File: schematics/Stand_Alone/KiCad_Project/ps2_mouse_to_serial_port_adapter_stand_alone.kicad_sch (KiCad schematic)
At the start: 24 parts, among them J1 Barrel Jack 2.1 mm, J2 DB9 Female, J3 Mini-DIN-6, Q1 BC547, SW1 1C2P, U1 74LS00, U2 L78L05, U3 L7805

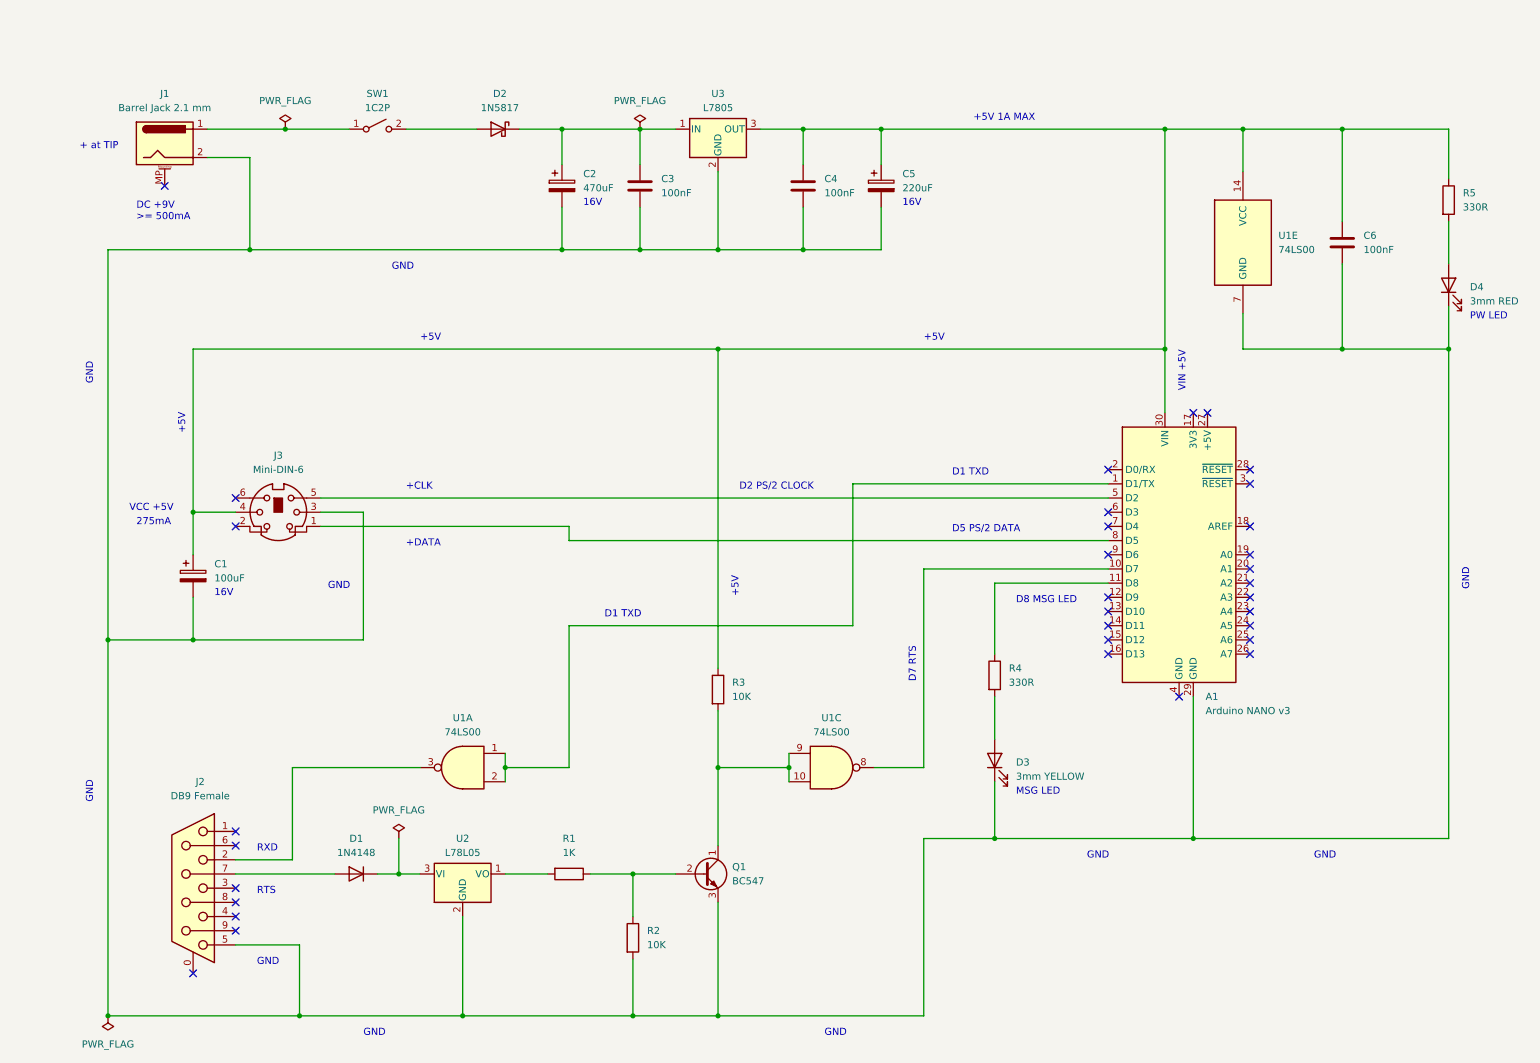
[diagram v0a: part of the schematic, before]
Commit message: v1.5.0
- Ajustadas las placas "Stand alone" y "In-a-box" al tamaño standard de
  90x70 mm.
- Añadidas a estas placas las zonas de relleno a masa (GND).
- Añadidas las serigrafias con los valores de todos los componentes en todas
  las versiones de las placas.
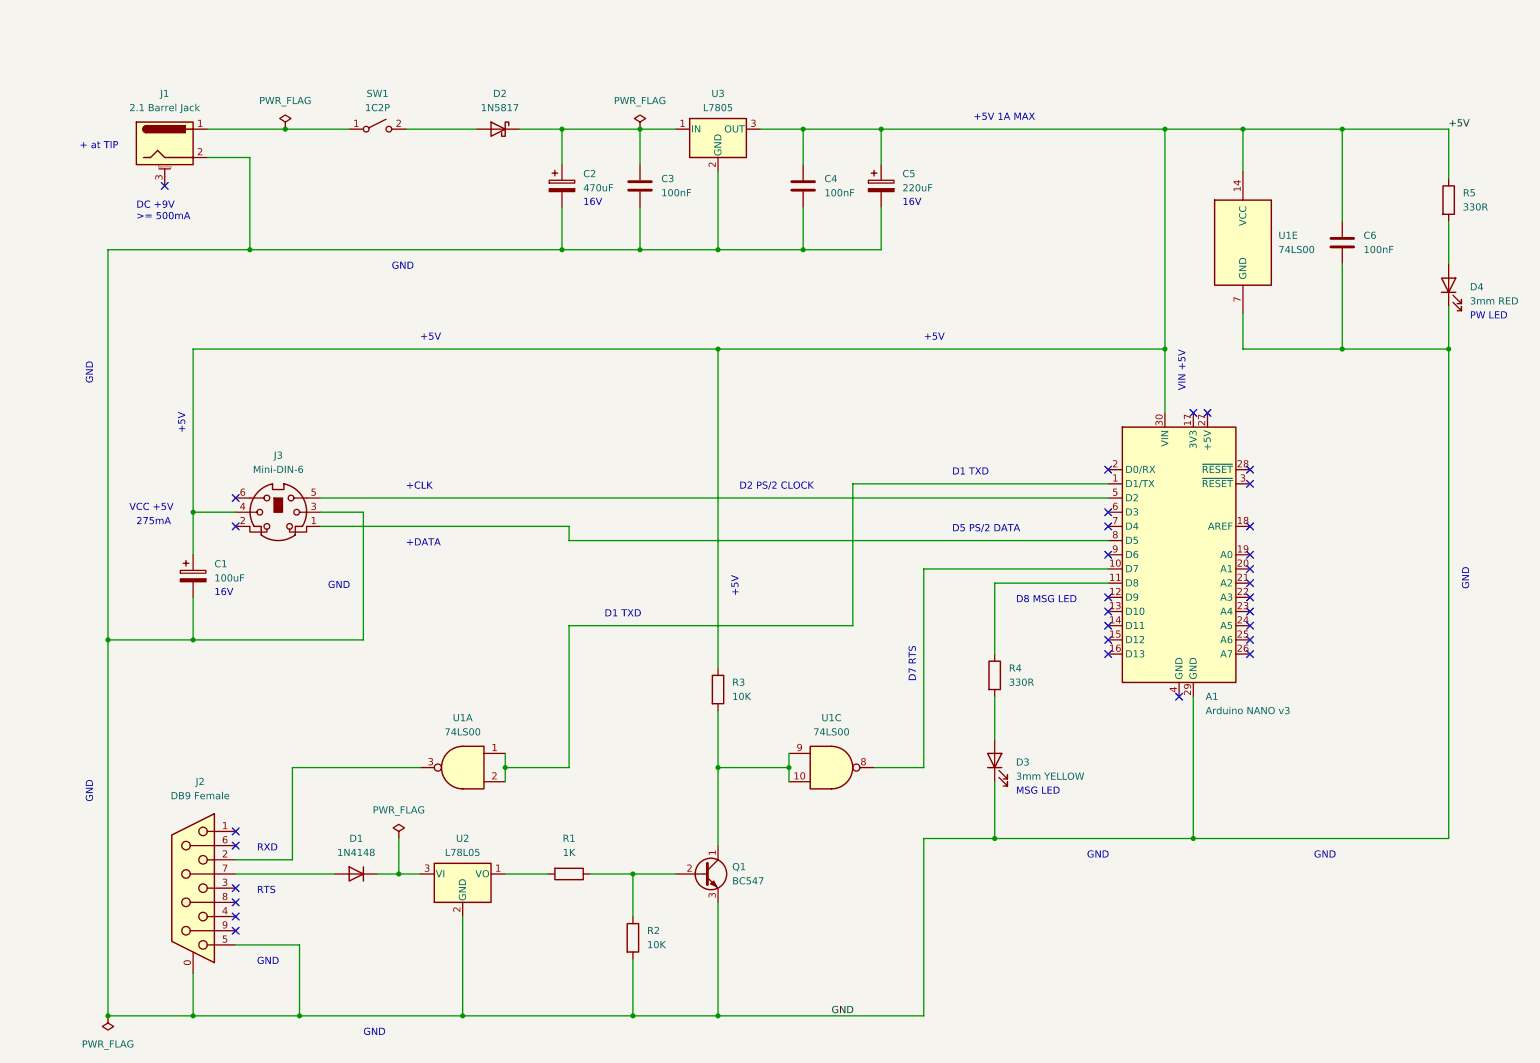
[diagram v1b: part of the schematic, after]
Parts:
- removed J1: Barrel Jack 2.1 mm, Connector_BarrelJack:BarrelJack_Horizontal, symbol Connector:Barrel_Jack_MountingPin
- added J1: 2.1 Barrel Jack, Connector_BarrelJack:BarrelJack_Kycon_KLDX-0202-xC_Horizontal, symbol CustomSymbols:Barrel_Jack_MountingPin
- U1: footprint (none) -> Package_DIP:DIP-14_W7.62mm_Socket
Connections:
- net +5V: now reaches A1.30 (VIN), C1.1, C4.1, C5.1, C6.1, J3.4, R3.1, R5.1, U1.14 (VCC), U3.3 (OUT)
- net GND: now reaches A1.29 (GND), C1.2, C2.2, C3.2, C4.2, C5.2, C6.2, D3.1 (K), D4.1 (K), J2.5, J3.3, Q1.3 (E), R2.2, U1.7 (GND), U2.2 (GND), U3.2 (GND)
- net GND: now also J2.0 (PAD), J1.2
- net at SW1.1 (A): now also J1.1
- no-connect marks 39 -> 38
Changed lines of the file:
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@@
   (title_block
     (title "PS/2 Mouse  to Serial Port Adapter")
-    (date "2023-08-12")
-    (rev "3")
+    (date "2023-08-13")
+    (rev "4")
     (company "Cesar Rincon")
     (comment 1 "NightFox & Co.")
@@
   (junction (at 212.09 64.77) (diameter 0) (color 0 0 0 0)
   )
+  (junction (at 38.1 184.15) (diameter 0) (color 0 0 0 0)
+  )
   (junction (at 181.61 152.4) (diameter 0) (color 0 0 0 0)
   )
@@
   (no_connect (at 219.71 76.2))
   (no_connect (at 227.33 114.3))
-  (no_connect (at 33.02 35.56))
   (no_connect (at 227.33 104.14))
   (no_connect (at -111.76 2.54))
@@
   (no_connect (at 201.93 111.76))
   (no_connect (at 214.63 127))
+  (no_connect (at 33.02 35.56))
   (no_connect (at -127 25.4))
   (no_connect (at 227.33 101.6))
@@
   (no_connect (at 201.93 101.6))
   (no_connect (at -111.76 27.94))
-  (no_connect (at 38.1 176.53))
   (no_connect (at 201.93 116.84))
   (no_connect (at 45.72 96.52))
@@
     (stroke (width 0) (type default))
   )
+  (wire (pts (xy 38.1 176.53) (xy 38.1 184.15))
+    (stroke (width 0) (type default))
+  )
   (wire (pts (xy 55.88 139.7) (xy 78.74 139.7))
     (stroke (width 0) (type default))
@@
     (stroke (width 0) (type default))
   )
+  (wire (pts (xy 48.26 30.48) (xy 48.26 46.99))
+    (stroke (width 0) (type default))
+  )
   (wire (pts (xy 104.14 46.99) (xy 118.11 46.99))
     (stroke (width 0) (type default))
@@
     (stroke (width 0) (type default))
   )
+  (wire (pts (xy 38.1 184.15) (xy 57.15 184.15))
+    (stroke (width 0) (type default))
+  )
   (wire (pts (xy 201.93 106.68) (xy 181.61 106.68))
     (stroke (width 0) (type default))
@@
     (stroke (width 0) (type default))
   )
-  (wire (pts (xy 22.86 184.15) (xy 57.15 184.15))
+  (wire (pts (xy 22.86 184.15) (xy 38.1 184.15))
     (stroke (width 0) (type default))
   )
@@
     (stroke (width 0) (type default))
   )
-  (wire (pts (xy 48.26 30.48) (xy 48.26 46.99))
-    (stroke (width 0) (type default))
-  )
   (wire (pts (xy 212.09 25.4) (xy 212.09 64.77))
     (stroke (width 0) (type default))
@@
     (effects (font (size 1.27 1.27)) (justify left bottom))
   )
-  (text "GND" (at 151.13 187.96 0)
-    (effects (font (size 1.27 1.27)) (justify left bottom))
-  )
   (text "GND" (at 49.53 175.26 0)
     (effects (font (size 1.27 1.27)) (justify left bottom))
@@
     (effects (font (size 1.27 1.27)) (justify left bottom))
   )
+  (label "+5V" (at 262.89 25.4 0) (fields_autoplaced)
+    (effects (font (size 1.27 1.27)) (justify left bottom))
+  )
+  (label "GND" (at 152.4 184.15 0) (fields_autoplaced)
+    (effects (font (size 1.27 1.27)) (justify left bottom))
+  )
   (symbol (lib_id "74xx:74LS00") (at -119.38 2.54 0) (unit 2)
     (in_bom yes) (on_board yes) (dnp no) (fields_autoplaced)
@@
       (effects (font (size 1.27 1.27)))
     )
-    (property "Footprint" "" (at -119.38 2.54 0)
+    (property "Footprint" "Package_DIP:DIP-14_W7.62mm_Socket" (at -119.38 2.54 0)
       (effects (font (size 1.27 1.27)) hide)
     )
@@
     )
   )
-  (symbol (lib_id "Connector:Barrel_Jack_MountingPin") (at 33.02 27.94 0) (unit 1)
-    (in_bom yes) (on_board yes) (dnp no) (fields_autoplaced)
-    (property "Reference" "J1" (at 33.02 19.05 0)
-      (effects (font (size 1.27 1.27)))
-    )
-    (property "Value" "Barrel Jack 2.1 mm" (at 33.02 21.59 0)
-      (effects (font (size 1.27 1.27)))
-    )
-    (property "Footprint" "Connector_BarrelJack:BarrelJack_Horizontal" (at 34.29 28.956 0)
-      (effects (font (size 1.27 1.27)) hide)
-    )
-    (property "Datasheet" "~" (at 34.29 28.956 0)
-      (effects (font (size 1.27 1.27)) hide)
-    )
-    (pin "1")
-    (pin "2")
-    (pin "MP")
-    (instances
-      (project "ps2_mouse_to_serial_port_adapter_stand_alone"
-        (path "/a7ffaf24-5f7f-4c3c-9493-bf517f6435f3"
-          (reference "J1") (unit 1)
-        )
-      )
-    )
-  )
   (symbol (lib_id "Connector:Mini-DIN-6") (at 53.34 93.98 0) (unit 1)
     (in_bom yes) (on_board yes) (dnp no) (fields_autoplaced)
@@
       (effects (font (size 1.27 1.27)))
     )
-    (property "Footprint" "" (at -119.38 27.94 0)
+    (property "Footprint" "Package_DIP:DIP-14_W7.62mm_Socket" (at -119.38 27.94 0)
       (effects (font (size 1.27 1.27)) hide)
     )
@@
         )
       )
+    )
+  )
+  (symbol (lib_id "CustomSymbols:Barrel_Jack_MountingPin") (at 33.02 27.94 0) (unit 1)
+    (in_bom yes) (on_board yes) (dnp no) (fields_autoplaced)
+    (property "Reference" "J1" (at 33.02 19.05 0)
+      (effects (font (size 1.27 1.27)))
+    )
+    (property "Value" "2.1 Barrel Jack" (at 33.02 21.59 0)
+      (effects (font (size 1.27 1.27)))
+    )
+    (property "Footprint" "Connector_BarrelJack:BarrelJack_Kycon_KLDX-0202-xC_Horizontal" (at 34.29 28.956 0)
+      (effects (font (size 1.27 1.27)) hide)
+    )
+    (property "Datasheet" "~" (at 34.29 28.956 0)
+      (effects (font (size 1.27 1.27)) hide)
+    )
+    (pin "1")
+    (pin "2")
+    (pin "3")
+    (instances
+      (project "ps2_mouse_to_serial_port_adapter_stand_alone"
+        (path "/a7ffaf24-5f7f-4c3c-9493-bf517f6435f3"
+          (reference "J1") (unit 1)
+        )
+      )

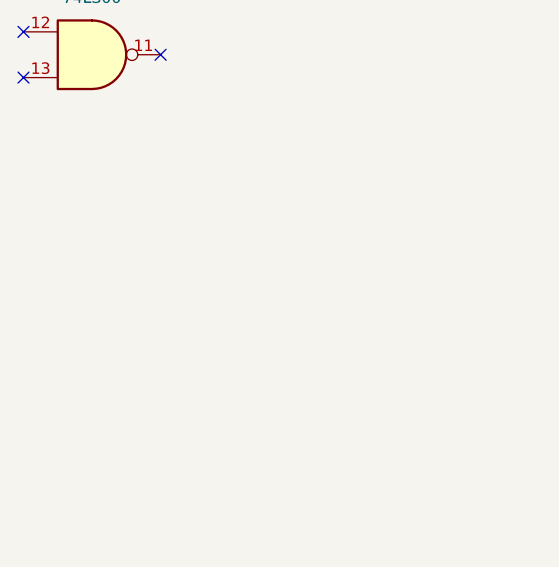
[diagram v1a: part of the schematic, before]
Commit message: v1.5.1
- Arreglada la serigrafía del conector MINI-DIN-6 (PS/2), la cual se superponía en algunas zonas de soldado.
- En todas las placas se añade el símbolo de los agujeros de montaje con el tamaño estándar M3.
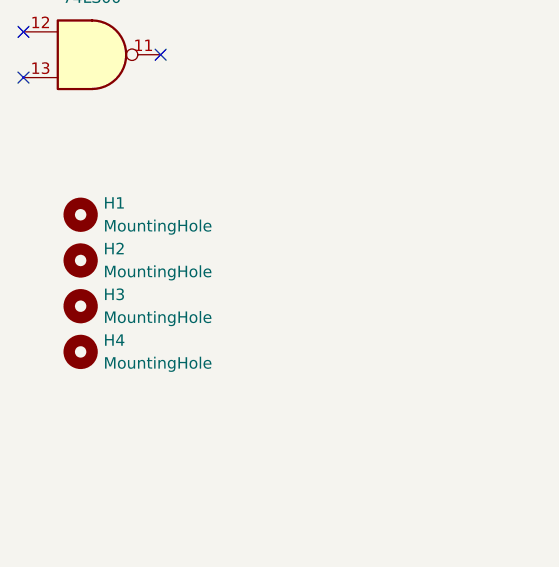
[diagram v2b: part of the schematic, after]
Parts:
- added H1, H2, H3, H4: MountingHole, MountingHole:MountingHole_3.2mm_M3, symbol Mechanical:MountingHole
- J3: footprint CustomFootPrints:Conn_Mini_DIN_6pin -> ProjectLibrary:Connector_Mini_DIN_6pin
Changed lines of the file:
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@@
   (title_block
     (title "PS/2 Mouse  to Serial Port Adapter")
-    (date "2023-08-13")
-    (rev "4")
+    (date "2023-08-14")
+    (rev "5")
     (company "Cesar Rincon")
     (comment 1 "NightFox & Co.")
@@
     )
   )
+  (symbol (lib_id "Mechanical:MountingHole") (at -120.65 50.8 0) (unit 1)
+    (in_bom yes) (on_board yes) (dnp no) (fields_autoplaced)
+    (property "Reference" "H2" (at -118.11 49.53 0)
+      (effects (font (size 1.27 1.27)) (justify left))
+    )
+    (property "Value" "MountingHole" (at -118.11 52.07 0)
+      (effects (font (size 1.27 1.27)) (justify left))
+    )
+    (property "Footprint" "MountingHole:MountingHole_3.2mm_M3" (at -120.65 50.8 0)
+      (effects (font (size 1.27 1.27)) hide)
+    )
+    (property "Datasheet" "~" (at -120.65 50.8 0)
+      (effects (font (size 1.27 1.27)) hide)
+    )
+    (instances
+      (project "ps2_mouse_to_serial_port_adapter_stand_alone"
+        (path "/a7ffaf24-5f7f-4c3c-9493-bf517f6435f3"
+          (reference "H2") (unit 1)
+        )
+      )
+    )
+  )
   (symbol (lib_id "Diode:1N5817") (at 92.71 25.4 0) (mirror y) (unit 1)
     (in_bom yes) (on_board yes) (dnp no) (fields_autoplaced)
@@
       (effects (font (size 1.27 1.27)))
     )
-    (property "Footprint" "CustomFootPrints:Conn_Mini_DIN_6pin" (at 53.34 93.98 0)
+    (property "Footprint" "ProjectLibrary:Connector_Mini_DIN_6pin" (at 53.34 93.98 0)
       (effects (font (size 1.27 1.27)) hide)
     )
@@
     )
   )
+  (symbol (lib_id "Mechanical:MountingHole") (at -120.65 45.72 0) (unit 1)
+    (in_bom yes) (on_board yes) (dnp no) (fields_autoplaced)
+    (property "Reference" "H1" (at -118.11 44.45 0)
+      (effects (font (size 1.27 1.27)) (justify left))
+    )
+    (property "Value" "MountingHole" (at -118.11 46.99 0)
+      (effects (font (size 1.27 1.27)) (justify left))
+    )
+    (property "Footprint" "MountingHole:MountingHole_3.2mm_M3" (at -120.65 45.72 0)
+      (effects (font (size 1.27 1.27)) hide)
+    )
+    (property "Datasheet" "~" (at -120.65 45.72 0)
+      (effects (font (size 1.27 1.27)) hide)
+    )
+    (instances
+      (project "ps2_mouse_to_serial_port_adapter_stand_alone"
+        (path "/a7ffaf24-5f7f-4c3c-9493-bf517f6435f3"
+          (reference "H1") (unit 1)
+        )
+      )
+    )
+  )
   (symbol (lib_id "Device:LED") (at 181.61 138.43 90) (unit 1)
     (in_bom yes) (on_board yes) (dnp no) (fields_autoplaced)
@@
         (path "/a7ffaf24-5f7f-4c3c-9493-bf517f6435f3"
           (reference "D3") (unit 1)
+        )
+      )
+    )
+  )
+  (symbol (lib_id "Mechanical:MountingHole") (at -120.65 55.88 0) (unit 1)
+    (in_bom yes) (on_board yes) (dnp no) (fields_autoplaced)
+    (property "Reference" "H3" (at -118.11 54.61 0)
+      (effects (font (size 1.27 1.27)) (justify left))
+    )
+    (property "Value" "MountingHole" (at -118.11 57.15 0)
+      (effects (font (size 1.27 1.27)) (justify left))
+    )
+    (property "Footprint" "MountingHole:MountingHole_3.2mm_M3" (at -120.65 55.88 0)
+      (effects (font (size 1.27 1.27)) hide)
+    )
+    (property "Datasheet" "~" (at -120.65 55.88 0)
+      (effects (font (size 1.27 1.27)) hide)
+    )
+    (instances
+      (project "ps2_mouse_to_serial_port_adapter_stand_alone"
+        (path "/a7ffaf24-5f7f-4c3c-9493-bf517f6435f3"
+          (reference "H3") (unit 1)
         )
       )
@@
         )
       )
+    )
+  )
+  (symbol (lib_id "Mechanical:MountingHole") (at -120.65 60.96 0) (unit 1)
+    (in_bom yes) (on_board yes) (dnp no) (fields_autoplaced)
+    (property "Reference" "H4" (at -118.11 59.69 0)
+      (effects (font (size 1.27 1.27)) (justify left))
+    )
+    (property "Value" "MountingHole" (at -118.11 62.23 0)
+      (effects (font (size 1.27 1.27)) (justify left))
+    )
+    (property "Footprint" "MountingHole:MountingHole_3.2mm_M3" (at -120.65 60.96 0)
+      (effects (font (size 1.27 1.27)) hide)
+    )
+    (property "Datasheet" "~" (at -120.65 60.96 0)
+      (effects (font (size 1.27 1.27)) hide)
+    )
+    (instances
+      (project "ps2_mouse_to_serial_port_adapter_stand_alone"
+        (path "/a7ffaf24-5f7f-4c3c-9493-bf517f6435f3"
+          (reference "H4") (unit 1)
+        )
+      )

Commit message: v1.7.0
- Modificadas las huellas de todas las placas para que los componentes TO92 resulten más fáciles de soldar a mano.
- Modificadas las conexiones del conector IDC en la placa ISA para poder usar un cable IDC a DB9 comercial, sin necesidad de realizarle modificaciones.
- Añadido el modelo en formato FreeCad y el archivo STL del soporte para la placa ISA. Estos archivos estan preparados para poder realizar la impresión en 3D del soporte. Se recomienda un in-fill del 100%.
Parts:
- Q1, U2: footprint Package_TO_SOT_THT:TO-92_Inline -> Package_TO_SOT_THT:TO-92_HandSolder
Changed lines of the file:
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@@
   (title_block
     (title "PS/2 Mouse  to Serial Port Adapter")
-    (date "2023-08-14")
-    (rev "5")
+    (date "2023-08-28")
+    (rev "6")
     (company "Cesar Rincon")
     (comment 1 "NightFox & Co.")
@@
       (effects (font (size 1.27 1.27)) (justify left))
     )
-    (property "Footprint" "Package_TO_SOT_THT:TO-92_Inline" (at 134.62 160.655 0)
+    (property "Footprint" "Package_TO_SOT_THT:TO-92_HandSolder" (at 134.62 160.655 0)
       (effects (font (size 1.27 1.27) italic) (justify left) hide)
     )
@@
       (effects (font (size 1.27 1.27)))
     )
-    (property "Footprint" "Package_TO_SOT_THT:TO-92_Inline" (at 86.36 153.035 0)
+    (property "Footprint" "Package_TO_SOT_THT:TO-92_HandSolder" (at 86.36 153.035 0)
       (effects (font (size 1.27 1.27) italic) hide)
     )
